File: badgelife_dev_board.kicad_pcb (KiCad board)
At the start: 2 copper layers, 33 x 42 mm, 14 parts, among them J1 Conn_01x08, J2 Conn_01x08, J3 Conn_01x09, J4 Conn_01x09, X1 Badgelife_shitty_connector

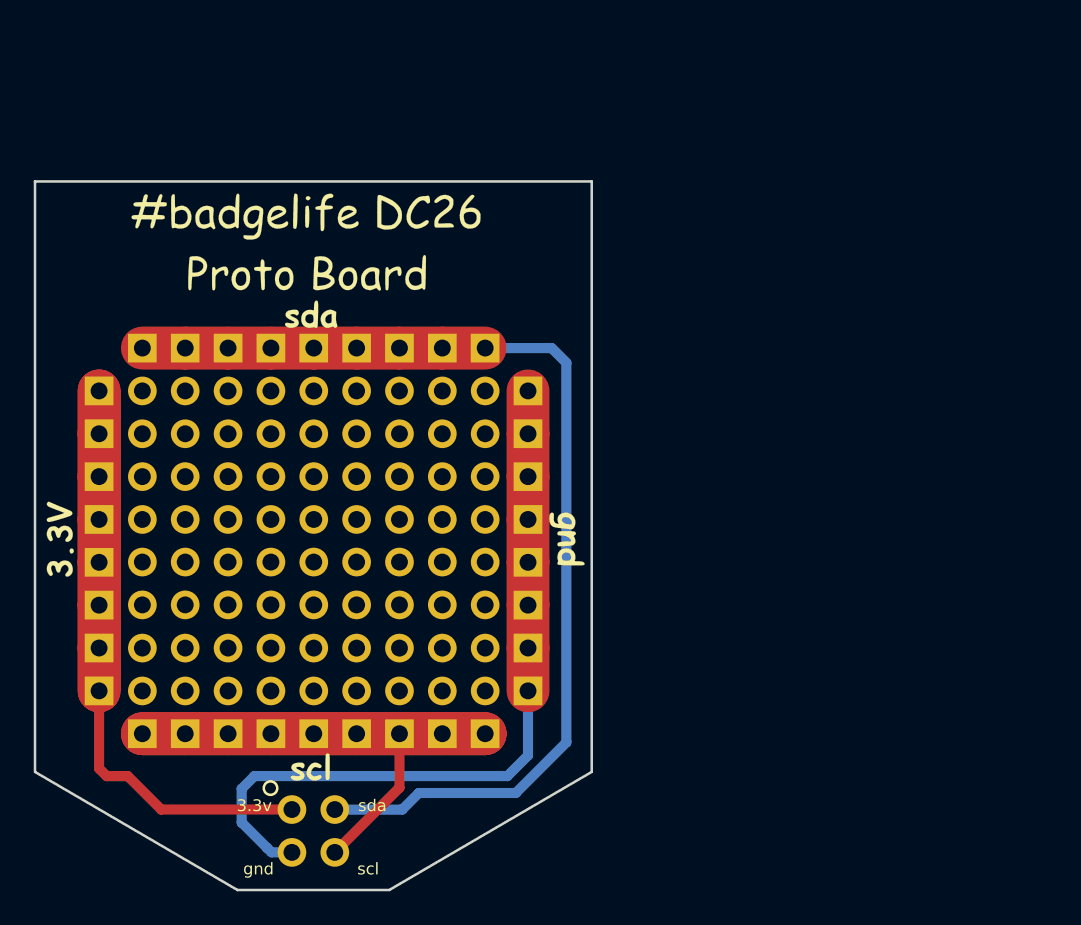
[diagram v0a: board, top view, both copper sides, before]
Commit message: add simple BioHacking Village artwork to add-on board
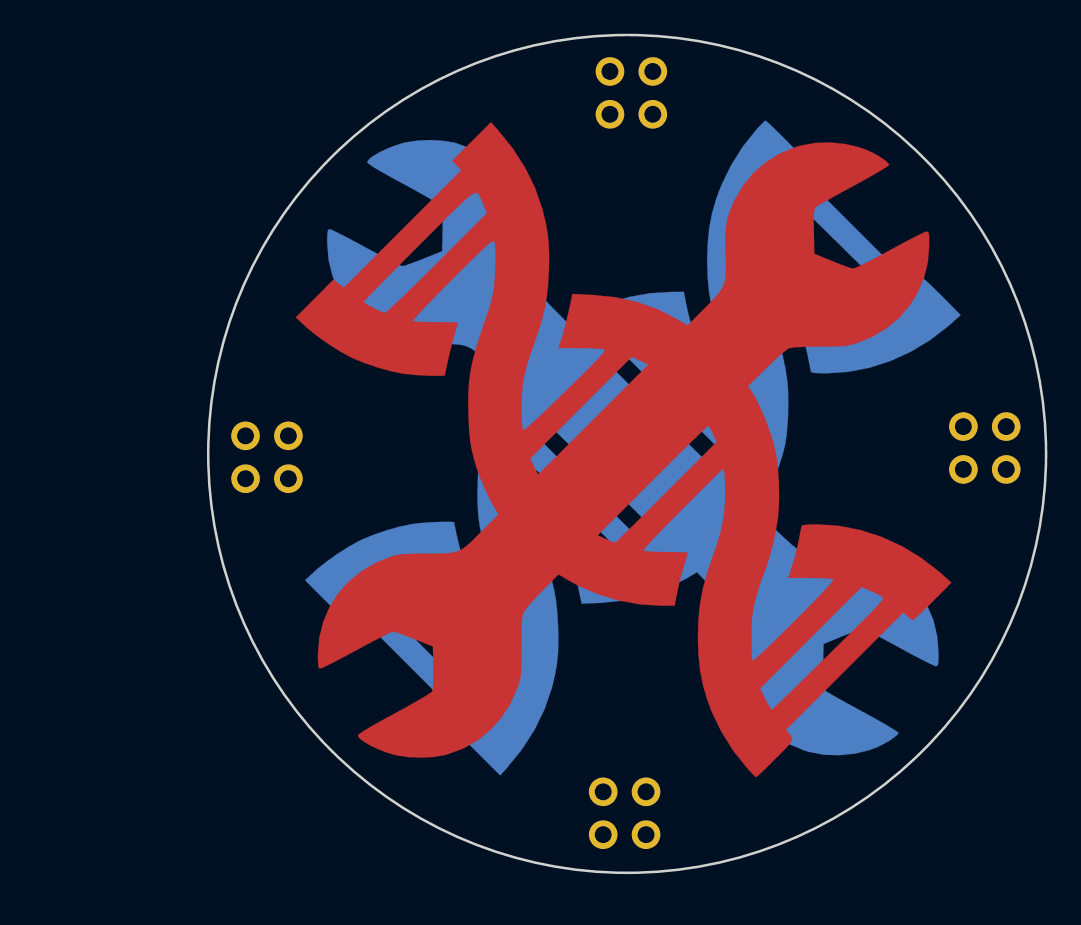
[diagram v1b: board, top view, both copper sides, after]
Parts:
- removed the G*** at (113.4, 162.2)
- removed the G*** at (128.2, 148.8)
- removed the G*** at (128.4, 175.7)
- removed the G*** at (143.7, 162.3)
- removed the G*** at (128.9, 144.6)
- removed J1, J2: Conn_01x08, mrmeeseeks:Power_Rail-01x08
- removed J3, J4: Conn_01x09, mrmeeseeks:Power_Rail-01x09
- removed REF** (x4): Pin_Header_Straight_2x09_Pitch2.54mm, mrmeeseeks:Pin_Header_Straight_2x09_Pitch2.54mm-NoSilk
- added G***: LOGO, badgelife_dev_board:wrench-neg-mask, B.Cu at (145.9, 156.1)
- added G***: LOGO, badgelife_dev_board:wrench-neg-mask, F.Cu at (145.4, 157.6)
- added G***: LOGO, badgelife_dev_board:wrench-neg, F.Cu at (145.4, 157.6)
- added G***: LOGO, badgelife_dev_board:wrench-neg, B.Cu at (146.0, 156.1)
- added X1: Badgelife_shitty_connector, mrmeeseeks:Badgelife-Shitty-2x2, B.Cu at (147.3, 135.8)
- added X1: Badgelife_shitty_connector, mrmeeseeks:Badgelife-Shitty-2x2, B.Cu at (168.3, 156.8)
- added X1: Badgelife_shitty_connector, mrmeeseeks:Badgelife-Shitty-2x2, B.Cu at (125.8, 157.3)
- X1: moved to B.Cu
- moved X1 18.5 mm to (146.9, 178.4)
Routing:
- net SDA: track 63.4 -> 0.00 mm
- net +3V3: track 52.6 -> 0.00 mm
- net SCL: track 49.3 -> 0.00 mm
- net GND: track 45.1 -> 0.00 mm
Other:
- board size 33 x 42 mm -> 49.7 x 49.7 mm
